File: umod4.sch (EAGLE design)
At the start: 94 parts, among them IC3 27C256-FEED-THRU, J1 DM3AT-SF-PEJ, J2 10118194-0001LF, M1 RPi Pico W, M2 Generic single-sided NEO-8, Q1 C10487/SI2301CDS, Q2 SS8050, Q3 C10487/SI2301CDS, Q4 C10487/SI2301CDS, U1 74LVC541, U2 74LVC4245, U3 74LVC541, U4 RP2040, U5 W25Q128JVSIQ, U6 74LVC2G04, U8 3.3V/150mA, Y1 12MHz

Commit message: 4v2a Release: add caps, DNP convention, production automation
Board changes:
- See Changelist-4V2.md for details

Tooling:
- Add preproduction.py: BOM generation (HTML + CSV), CPL generation via Eagle ULP batch mode, gerber freshness check, and ZIP packaging
- Add jlcpcb_smta_exporter_v7.ulp: modified to accept batch-mode arguments, bypassing interactive dialogs when invoked from script
- Update jlcpcb_2_layer_v72.cam: output path changed to build/cam/
- Update .gitignore: build/ directory rules with build/cam/.gitkeep anchor

Documentation:
- Add Production.md: describes end-to-end JLCPCB submission workflow
- Remove TestPlan.md
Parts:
- removed D4: C2761795/WS2812B, SparkFun-LED:WS2812B
- removed J2: 10118194-0001LF, 10118194-0001LF:10118194-0001LF
- removed JP5, JP6: JUMPER-SMT_3_1-NC_TRACE_NO-SILK, SparkFun-Jumpers:JUMPER-SMT_3_1-NC_TRACE_NO-SILK
- removed Q3, Q4: C10487/SI2301CDS, robins-v7:FET-P-CHANNELSI2369DS
- removed S1: (no value), robins-v7:SWITCH-TAC-5.2MM
- added C25: 100n/16V/X7R, SparkFun-03-01-2010:CAP0402-CAP
- added LED5: WS2812, SparkFun-LED:WS2812B
- added LED7: NCD0805R1, led:LEDSML0805
- added R26: 10K, SparkFun-03-01-2010:RESISTOR0402-RES
- added R27: 1K, SparkFun-03-01-2010:RESISTOR0402-RES
- added R28: 470R, SparkFun-03-01-2010:RESISTOR0402-RES
- added TP10, TP11, TP12, TP13, TP14, TP15, TP16: 1035, robins-v7:TEST-POINT-1035
- added U7: 74LVC4245, robins-v7:74LVC4245-TSSOP24
- C10, C3: value 100n/16V/X7R -> 2u2/6.3V/X5R; LCSC_PART C1525 -> C12530
- C11: value 100n/16V/X7R -> 33p/6.3V/COG; LCSC_PART C1525 -> C1562
- C13: value 1u/25V/X5R -> 4u7/10V/X5R; LCSC_PART C52923 -> C23733
- C16, C24: value 100n/16V/X7R -> 10u/25V/X5R; device SparkFun-03-01-2010:CAP0402-CAP -> robins-v7:CAP-0805; LCSC_PART C1525 -> C15850
- C17: value 33p/6.3V/COG -> 10u/25V/X5R; device SparkFun-03-01-2010:CAP0402-CAP -> robins-v7:CAP-0805; LCSC_PART C1562 -> C15850
- C2, C28: value 1u/25V/X5R -> 100n/16V/X7R; LCSC_PART C52923 -> C1525
- C20, C22: value 2u2/6.3V/X5R -> 100n/16V/X7R; LCSC_PART C12530 -> C1525
- C21: value 2u2/6.3V/X5R -> 1u/25V/X5R; LCSC_PART C12530 -> C52923
- C23: value 100n/16V/X7R -> 1u/25V/X5R; LCSC_PART C1525 -> C52923
- C26: value 100n/16V/X7R -> 4u7/10V/X5R; LCSC_PART C1525 -> C23733
- C27: value 4u7/10V/X5R -> 100n/16V/X7R; LCSC_PART C23733 -> C1525
- C4: value 1u/25V/X5R -> 2u2/6.3V/X5R; LCSC_PART C52923 -> C12530
- D2: value C2761795/WS2812B -> 1N5819WS; device SparkFun-LED:WS2812B -> SparkFun-DiscreteSemi:DIODE-SCHOTTKY-BAT20J; LCSC_PART C2761795 -> C191023
- JP1: value PINHD-1X12 -> (none); device robins:PINHD-1X12 -> pinhead:PINHD-1X3
- JP4: value (none) -> PINHD-1X12; device pinhead:PINHD-1X3 -> robins:PINHD-1X12
- LED3: value KT-0805G -> KT-0805Y; LCSC_PART C2297 -> C2296
- LED6: value C2761795/WS2812B -> WS2812; LCSC_PART C2761795 -> C42417498
- M1: value RPi Pico W -> Generic single-sided NEO-8; device robins-v7:PICO-OR-PICOW'-PICO-OR-W' -> robins-v7:GPS-GENERIC-DS-DBL-SIDED
- M2: value Generic single-sided NEO-8 -> RPi Pico W; device robins-v7:GPS-GENERIC-DS-DBL-SIDED -> robins-v7:PICO-OR-PICOW'-PICO-OR-W'
- Q1: value C10487/SI2301CDS -> DNP/SI2301CDS; DNP_LCSC_PART (none) -> C10487; LCSC_PART C10487 -> (none)
- R1: value 1K -> 100R; device SparkFun-03-01-2010:RESISTOR0402-RES -> SparkFun-03-01-2010:RESISTOR0603-RES; LCSC_PART C11702 -> C22775
- R10: value 27R -> 1K; LCSC_PART C25100 -> C11702
- R11, R18: value 27R -> 10K; LCSC_PART C25100 -> C25744
- R13, R25: value 1K -> 10K; LCSC_PART C11702 -> C25744
- R14, R6: value 10K -> 1K; LCSC_PART C25744 -> C11702
- R2: device SparkFun-03-01-2010:RESISTOR0402-RES -> SparkFun-03-01-2010:RESISTOR0603-RES; LCSC_PART (none) -> C22775
- R20: value 470R -> 100R; device SparkFun-03-01-2010:RESISTOR0402-RES -> SparkFun-03-01-2010:RESISTOR0603-RES; LCSC_PART C25117 -> C22775
- R23: value 1K -> 470R; LCSC_PART C11702 -> C25117
- R24: value 10K -> 470R; LCSC_PART C25744 -> C25117
- R4: value 1K -> 4K7; device SparkFun-03-01-2010:RESISTOR0402-RES -> SparkFun-03-01-2010:RESISTOR0603-RES; LCSC_PART C11702 -> C23162
- R7: value 470R -> 10K; LCSC_PART C25117 -> C25744
- R9: value 100R -> 10K; LCSC_PART (none) -> C25744
- SD1: value DM3AT-SF-PEJ -> DM3AT-SF-PEJM5; LCSC_PART (none) -> C114218; SKIP_LCSC_PART C114218 -> (none)
- TP1, TP2, TP3, TP4, TP5, TP6, TP7, TP8, TP9: value (none) -> 1035
- U1: value 74LVC541 -> RP2040; device robins-v7:74XX541-TSSOP20 -> robins-v7:RP2040-QFN56; LCSC_PART C113281 -> C2040
- U2: value 74LVC4245 -> W25Q128JVSIQ; device robins-v7:74LVC4245-TSSOP24 -> SparkFun-IC-Memory:W25Q32FVSS; LCSC_PART C6091 -> C97521
- U3: value 74LVC541 -> SY6280AAC; device robins-v7:74XX541-TSSOP20 -> robins-v7:HI-SIDE-SW; LCSC_PART C113281 -> C55136
- U4: value RP2040 -> 74LVC2G04; device robins-v7:RP2040-QFN56 -> robins-v7:74LVC2G04-SOT23-6; LCSC_PART C2040 -> C10428
- U5: value W25Q128JVSIQ -> 74LVC541; device SparkFun-IC-Memory:W25Q32FVSS -> robins-v7:74XX541-TSSOP20; LCSC_PART C97521 -> C113281
- U6: value 74LVC2G04 -> 74LVC541; device robins-v7:74LVC2G04-SOT23-6 -> robins-v7:74XX541-TSSOP20; LCSC_PART C10428 -> C113281
- U8: value 3.3V/150mA -> TLV75733P; LCSC_PART (none) -> C485517
- renumbered D3 to LED6, IC3 to IC1, J1 to SD1
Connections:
- removed net 3V3_GPS_EN: M1.GP5, R22.1, R23.2
- removed net 3V3_SD_EN: M1.GP22, R24.2, R25.1
- removed net 3V3_SD_SW: JP5.3, Q4.S
- removed net 3V3_SW: JP6.3, Q3.S
- removed net N$15: R10.2, U4.USB_DP
- removed net N$16: R9.1, U4.SWD
- removed net N$17: J2.2, R11.1
- removed net N$18: J2.3, R10.1
- removed net N$23: Q4.G, R25.2
- removed net N$25: Q3.G, R23.1
- removed net SPARE0: LED3.C, M1.GP27, TP7.TP
- removed net SPARE1: LED4.C, M1.GP26, TP8.TP
- removed net SPARE2: M1.GP16, TP9.TP
- removed net VCC_GPS: JP6.2, M2.VCC, R8.2
- new net DISK_BSY: LED1.C, M2.GP26, TP5.TP
- new net EN_VDD_SD: M2.GP19, R17.1, U3.EN
- new net EP_BOOTSEL: M2.GP21, R6.2
- new net EP_SWD_DIS: JP3.1, M2.GP5
- new net EXT_RP_SWCLK: JP1.1, R1.2
- new net EXT_RP_SWD: JP1.3, R2.2
- new net SPARE0_ADC: M2.GP27, TP9.TP
- new net SPARE3: LED2.C, M2.GP16, TP10.TP
- new net SPARE4: LED7.C, M2.GP17, TP8.TP
- new net SPARE5: M2.GP18, TP6.TP
- new net SPARE6_ADC: M2.GP28, TP15.TP
- new net VCCB_PWR: M2.GP20, R26.2
- new net VLED: C27.1, C28.1, D2.C, LED5.VDD, LED6.VDD
- net !CARD: now also M2.GP6; no longer M1.GP6
- net !CE!_5V: now also R22.1, U4G$2.I, U7.!OE; no longer R6.1, U2.!OE, U6G$2.I
- net !RESET!_5V: now also JP4.6; no longer JP1.6
- net !RESET!_HC11_OUT: now also R25.1, U1.GPIO28_ADC2; no longer M1.GP28, R5.1, U4.GPIO28_ADC2
- net +3V3: now also C14.1, C17.1, C2.1, C4.1, C5.1, C6.1, C8.1, M1.VCC, M2.3V3(OUT), M2.ADC_REF, R11.1, R12.1, R19.2, R23.1, R24.1, R25.2, R28.1, R4.1, R7.2, U1.ADC_AVDD, U1.IOVDD0, U1.IOVDD1, U1.IOVDD2, U1.IOVDD3, U1.IOVDD4, U1.IOVDD5, U1.USB_VDD, U1.VREG_IN, U2.VCC, U3.IN; no longer C11.1, C12.1, C19.1, C20.1, C22.1, JP5.1, JP6.1, M1.3V3(OUT), M1.ADC_REF, Q3.D, Q4.D, R12.2, R17.1, R19.1, R20.1, R22.2, R3.2, R7.1, U4.ADC_AVDD, U4.IOVDD0, U4.IOVDD1, U4.IOVDD2, U4.IOVDD3, U4.IOVDD4, U4.IOVDD5, U4.USB_VDD, U4.VREG_IN, U5.VCC
- net +5_ECU: now also C25.1, C26.1, JP4.10, JP4.12, R22.2, U7.VCCA; no longer C28.1, C5.1, JP1.10, JP1.12, R6.2, U2.VCCA
- net 1.0V: now also C1.1, C3.1, U1.DVDD0, U1.DVDD1, U1.VREG_OUT; no longer C21.1, C8.1, U4.DVDD0, U4.DVDD1, U4.VREG_OUT
- net A0_5V: now also U5.A1; no longer U1.A1
- net A10_5V: now also U6.A3; no longer U3.A3
- net A11_5V: now also U6.A4; no longer U3.A4
- net A12_5V: now also U6.A5; no longer U3.A5
- net A13_5V: now also U6.A6; no longer U3.A6
- net A14_5V: now also U6.A7; no longer U3.A7
- net A1_5V: now also U5.A2; no longer U1.A2
- net A2_5V: now also U5.A3; no longer U1.A3
- net A3_5V: now also U5.A4; no longer U1.A4
- net A4_5V: now also U5.A5; no longer U1.A5
- net A5_5V: now also U5.A6; no longer U1.A6
- net A6_5V: now also U5.A7; no longer U1.A7
- net A7_5V: now also U5.A8; no longer U1.A8
- net A8_5V: now also U6.A1; no longer U3.A1
- net A9_5V: now also U6.A2; no longer U3.A2
- net CE: now also U1.GPIO26_ADC0, U4G$2.O; no longer U4.GPIO26_ADC0, U6G$2.O
- net D0: now also U1.GPIO16, U7.B1; no longer U2.B1, U4.GPIO16
- net D0_5V: now also U7.A1; no longer U2.A1
- net D1: now also U1.GPIO17, U7.B2; no longer U2.B2, U4.GPIO17
- net D1_5V: now also U7.A2; no longer U2.A2
- net D2: now also U1.GPIO18, U7.B3; no longer U2.B3, U4.GPIO18
- net D2_5V: now also U7.A3; no longer U2.A3
- net D3: now also U1.GPIO19, U7.B4; no longer U2.B4, U4.GPIO19
- net D3_5V: now also U7.A4; no longer U2.A4
- net D4: now also U1.GPIO20, U7.B5; no longer U2.B5, U4.GPIO20
- net D4_5V: now also U7.A5; no longer U2.A5
- net D5: now also U1.GPIO21, U7.B6; no longer U2.B6, U4.GPIO21
- net D5_5V: now also U7.A6; no longer U2.A6
- net D6: now also U1.GPIO22, U7.B7; no longer U2.B7, U4.GPIO22
- net D6_5V: now also U7.A7; no longer U2.A7
- net D7: now also U1.GPIO23, U7.B8; no longer U2.B8, U4.GPIO23
- net D7_5V: now also U7.A8; no longer U2.A8
- net DAT1: now also M2.GP13, R8.1; no longer M1.GP13, R16.1
- net DAT2: now also M2.GP14; no longer M1.GP14
- net DBG_BSY: now also LED4.C, TP14.TP, U1.GPIO29_ADC3; no longer D4.DI, LED1.C, TP1.TP, U4.GPIO29_ADC3
- net E: now also R20.1, U1.GPIO15; no longer R18.1, U4.GPIO15
- net EP_RUN: now also M2.GP4, R19.1, U1.RUN; no longer M1.GP4, R3.1, U4.RUN
- net E_5V: now also JP4.9, TP11.TP, U6.A8; no longer JP1.9, TP5.TP, U3.A8
- net GND: now also C11.1, C17.2, C25.2, JP1.2, JP3.2, JP4.1, JP4.3, LED3.C, LED5.VSS, M2.SWGND, R16.2, R17.2, R18.2, R3.2, TP1.TP, TP13.TP, TP16.TP, TP7.TP, U1.TESTEN, U2.GND, U4G$3.GND, U5.!OE1, U5.!OE2, U6.!OE1, U6.!OE2, U6.GND, U7.GND@1, U7.GND@2, U7.GND@3; no longer C11.2, C17.1, D2.VSS, D4.VSS, J2.5, JP1.1, JP1.3, JP4.2, LED2.C, M1.SWGND, R13.2, R14.2, R24.1, TP2.TP, TP3.TP, TP4.TP, U1.!OE1, U1.!OE2, U2.GND@1, U2.GND@2, U2.GND@3, U3.!OE1, U3.!OE2, U4.GND, U4.TESTEN, U6G$3.GND
- net GPS_PPS: now also M1.PPS, M2.GP7; no longer M1.GP7, M2.PPS
- net IO0: now also U1.GPIO0, U5.Y1; no longer U1.Y1, U4.GPIO0
- net IO1: now also U1.GPIO1, U5.Y2; no longer U1.Y2, U4.GPIO1
- net IO10: now also U1.GPIO10, U6.Y3; no longer U3.Y3, U4.GPIO10
- net IO11: now also U1.GPIO11, U6.Y4; no longer U3.Y4, U4.GPIO11
- net IO12: now also U1.GPIO12, U6.Y5; no longer U3.Y5, U4.GPIO12
- net IO13: now also U1.GPIO13, U6.Y6; no longer U3.Y6, U4.GPIO13
- net IO14: now also U1.GPIO14, U6.Y7; no longer U3.Y7, U4.GPIO14
- net IO2: now also U1.GPIO2, U5.Y3; no longer U1.Y3, U4.GPIO2
- net IO3: now also U1.GPIO3, U5.Y4; no longer U1.Y4, U4.GPIO3
- net IO4: now also U1.GPIO4, U5.Y5; no longer U1.Y5, U4.GPIO4
- net IO5: now also U1.GPIO5, U5.Y6; no longer U1.Y6, U4.GPIO5
- net IO6: now also U1.GPIO6, U5.Y7; no longer U1.Y7, U4.GPIO6
- net IO7: now also U1.GPIO7, U5.Y8; no longer U1.Y8, U4.GPIO7
- net IO8: now also U1.GPIO8, U6.Y1; no longer U3.Y1, U4.GPIO8
- net IO9: now also U1.GPIO9, U6.Y2; no longer U3.Y2, U4.GPIO9
- net N$1: now also R10.2; no longer R4.2
- net N$10: now also U1.QSPI_SD1, U2.SO(D1); no longer U4.QSPI_SD1, U5.SO(D1)
- net N$11: now also U1.QSPI_SD2, U2.!WP!(D2); no longer U4.QSPI_SD2, U5.!WP!(D2)
- net N$12: now also U1.QSPI_SD3, U2.!HOLD!(D3); no longer U4.QSPI_SD3, U5.!HOLD!(D3)
- net N$13: now also LED2.A, R23.2; no longer R11.2, U4.USB_DM
- net N$14: now also R16.1, U3.ISET; no longer R13.1, S1.1
- net N$19: now also LED5.DI; no longer D2.DI
- net N$2: now also C11.2, U1.XIN; no longer C17.2, U4.XIN
- net N$20: now also R20.2, U6.Y8; no longer R18.2, U3.Y8
- net N$21: now also LED1.A, R21.2; no longer LED3.A, R20.2
- net N$22: now also LED7.A, R28.2; no longer LED4.A, R21.2
- net N$3: now also LED3.A, R27.2; no longer LED2.A, R1.2
- net N$4: now also R14.1, TP4.TP; no longer R2.1, U4.SWCLK
- net N$5: now also R10.1, U1.XOUT; no longer R4.1, U4.XOUT
- net N$6: now also LED4.A, R24.2; no longer LED1.A, R7.2
- net N$7: now also R14.2, R6.1, R7.1, U1.QSPI_SS, U2.!CS!; no longer R12.1, S1.2, U4.QSPI_SS, U5.!CS!
- net N$8: now also U1.QSPI_SCLK, U2.SCK; no longer U4.QSPI_SCLK, U5.SCK
- net N$9: now also U1.QSPI_SD0, U2.SI(D0); no longer U4.QSPI_SD0, U5.SI(D0)
- net PICOW_U0_RX: now also M2.GP1, R11.2, TP2.TP, U1.GPIO24; no longer JP3.1, M1.GP1, R17.2, U4.GPIO24
- net PICOW_U0_TX: now also M2.GP0, R12.2, TP3.TP, U1.GPIO25; no longer JP3.2, M1.GP0, R19.2, U4.GPIO25
- net PICOW_U1_RX: now also M1.TX_OUT, M2.GP9; no longer M1.GP9, M2.TX_OUT
- net PICOW_U1_TX: now also M1.RX_IN, M2.GP8, R5.1; no longer M1.GP8, M2.RX_IN, R8.1
- net R/!W!_5V: now also JP4.8, TP12.TP, U4G$1.I; no longer JP1.8, TP6.TP, U6G$1.I
- net RP_SWCLK: now also M2.GP2, R1.1, R3.1, U1.SWCLK; no longer JP4.1, M1.GP2, R2.2
- net RP_SWD: now also M2.GP3, R2.1, R4.2, U1.SWD; no longer JP4.3, M1.GP3, R9.2
- net SPI1_CS: now also M2.GP15, R13.1; no longer M1.GP15
- net SPI1_MISO: now also M2.GP12, R9.1; no longer M1.GP12
- net SPI1_MOSI: now also M2.GP11; no longer M1.GP11
- net SPI1_SCK: now also M2.GP10, R18.1; no longer M1.GP10, R14.1
- net VBUS: now also M2.VBUS; no longer M1.VBUS
- net VCCB: now also C19.1, C20.1, C21.1, C22.1, C23.1, C24.1, R26.1, R27.1, U4G$3.VCC, U5.VCC, U6.VCC, U7.VCCB@1, U7.VCCB@2; no longer C1.1, C13.1, C2.1, C3.1, C4.1, C6.1, R1.1, U1.VCC, U2.VCCB@1, U2.VCCB@2, U3.VCC, U6G$3.VCC
- net VDD_SD: now also C12.1, C13.1, R13.2, R8.2, R9.2, U3.OUT; no longer C14.1, C27.1, JP5.2, R16.2
- net VSYS: now also D2.A, M2.VSYS; no longer C23.1, C24.1, C26.1, D2.VDD, D4.VDD, LED6.VDD, M1.VSYS
- net W/!R!: now also U1.GPIO27_ADC1, U4G$1.O, U7.DIR; no longer U2.DIR, U4.GPIO27_ADC1, U6G$1.O
- net WP_RUN: now also M2.RUN; no longer M1.RUN
- net WS2812_DI: now also M2.GP22; no longer M1.GP21
- net XIRQ_5V: now also JP4.4; no longer JP1.4
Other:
- note added: "ADC Capable"
- note added: "FET Q1 is optional Leaving it unstuffed increases the load on the ECU power supply a tiny bit, but leaving the FET out is one less part to break."
- note added: "GRN"
- note added: "RED"
- note added: "YEL"
- note removed: "BOOTSEL"
- note removed: "Default is that the RP2040 runs at boot, but can be reset by the Pico W if desired."
- note removed: "Default is to power SD Card via 3V3_SD_SW. If desired, cut the jumper and solder the other side to power SD card permanently via +3V3."
- note removed: "Default: DISABLED '1': ENABLED"
- note removed: "Default: ENABLED '0': DISABLED"

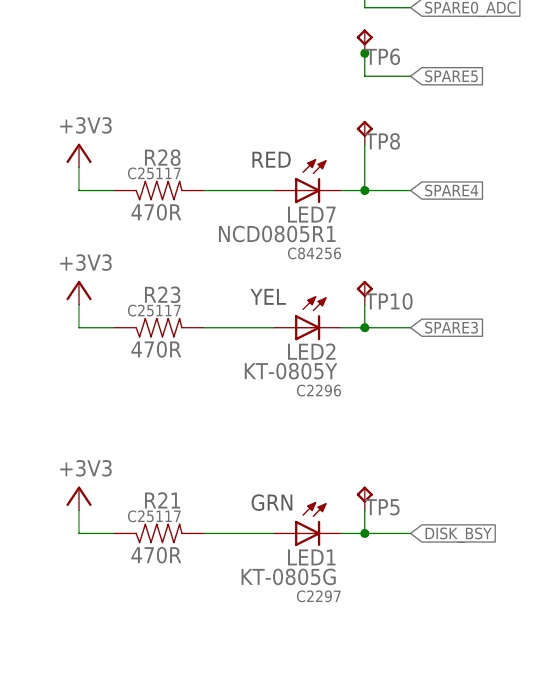
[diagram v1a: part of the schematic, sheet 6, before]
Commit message: Replace 470R 0402 package with SMD-0603-NOM
- Affected parts: R21, R23, R24, R28
- LCSC_PART changes from C25117 to C23179
- Manually reworked wire angles on board to clear DRC failures
  from the new pad geometry
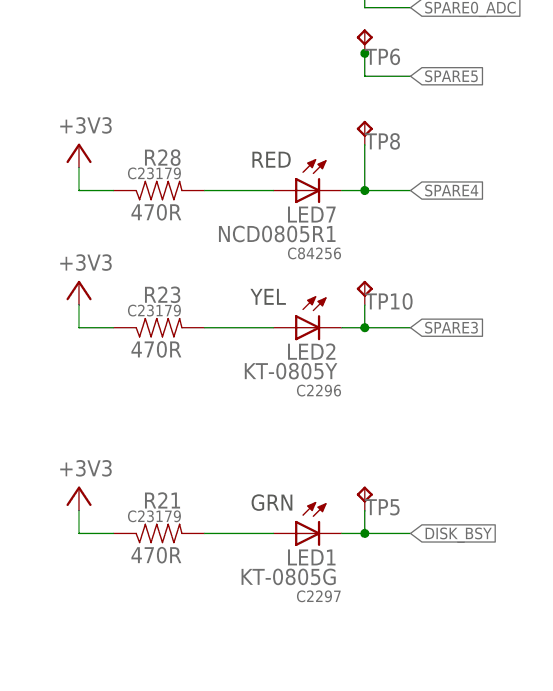
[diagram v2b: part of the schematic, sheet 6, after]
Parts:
- R21, R23, R24, R28: device SparkFun-03-01-2010:RESISTOR0402-RES -> robins-v7:RES-0603-NOM; LCSC_PART C25117 -> C23179
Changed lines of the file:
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@@
 <grid distance="0.1" unitdist="inch" unit="inch" style="lines" multiple="1" display="no" altdistance="0.01" altunitdist="inch" altunit="inch"/>
 <layers>
-<layer number="1" name="Top" color="4" fill="1" visible="yes" active="no"/>
-<layer number="2" name="Route2" color="1" fill="3" visible="yes" active="no"/>
-<layer number="3" name="Route3" color="4" fill="3" visible="yes" active="no"/>
-<layer number="14" name="Route14" color="1" fill="6" visible="yes" active="no"/>
-<layer number="15" name="Route15" color="4" fill="6" visible="yes" active="no"/>
-<layer number="16" name="Bottom" color="1" fill="1" visible="yes" active="no"/>
-<layer number="17" name="Pads" color="2" fill="1" visible="yes" active="no"/>
-<layer number="18" name="Vias" color="2" fill="1" visible="yes" active="no"/>
-<layer number="19" name="Unrouted" color="6" fill="1" visible="yes" active="no"/>
-<layer number="20" name="Dimension" color="15" fill="1" visible="yes" active="no"/>
-<layer number="21" name="tPlace" color="7" fill="1" visible="yes" active="no"/>
-<layer number="22" name="bPlace" color="7" fill="1" visible="yes" active="no"/>
-<layer number="23" name="tOrigins" color="15" fill="1" visible="yes" active="no"/>
-<layer number="24" name="bOrigins" color="15" fill="1" visible="yes" active="no"/>
-<layer number="25" name="tNames" color="7" fill="1" visible="yes" active="no"/>
-<layer number="26" name="bNames" color="7" fill="1" visible="yes" active="no"/>
-<layer number="27" name="tValues" color="7" fill="1" visible="yes" active="no"/>
-<layer number="28" name="bValues" color="7" fill="1" visible="yes" active="no"/>
+<layer number="1" name="Top" color="4" fill="1" visible="no" active="no"/>
+<layer number="2" name="Route2" color="1" fill="3" visible="no" active="no"/>
+<layer number="3" name="Route3" color="4" fill="3" visible="no" active="no"/>
+<layer number="14" name="Route14" color="1" fill="6" visible="no" active="no"/>
+<layer number="15" name="Route15" color="4" fill="6" visible="no" active="no"/>
+<layer number="16" name="Bottom" color="1" fill="1" visible="no" active="no"/>
+<layer number="17" name="Pads" color="2" fill="1" visible="no" active="no"/>
+<layer number="18" name="Vias" color="2" fill="1" visible="no" active="no"/>
+<layer number="19" name="Unrouted" color="6" fill="1" visible="no" active="no"/>
+<layer number="20" name="Dimension" color="15" fill="1" visible="no" active="no"/>
+<layer number="21" name="tPlace" color="7" fill="1" visible="no" active="no"/>
+<layer number="22" name="bPlace" color="7" fill="1" visible="no" active="no"/>
+<layer number="23" name="tOrigins" color="15" fill="1" visible="no" active="no"/>
+<layer number="24" name="bOrigins" color="15" fill="1" visible="no" active="no"/>
+<layer number="25" name="tNames" color="7" fill="1" visible="no" active="no"/>
+<layer number="26" name="bNames" color="7" fill="1" visible="no" active="no"/>
+<layer number="27" name="tValues" color="7" fill="1" visible="no" active="no"/>
+<layer number="28" name="bValues" color="7" fill="1" visible="no" active="no"/>
 <layer number="29" name="tStop" color="7" fill="3" visible="no" active="no"/>
 <layer number="30" name="bStop" color="7" fill="6" visible="no" active="no"/>
@@
 <layer number="35" name="tGlue" color="7" fill="4" visible="no" active="no"/>
 <layer number="36" name="bGlue" color="7" fill="5" visible="no" active="no"/>
-<layer number="37" name="tTest" color="7" fill="1" visible="yes" active="no"/>
-<layer number="38" name="bTest" color="7" fill="1" visible="yes" active="no"/>
+<layer number="37" name="tTest" color="7" fill="1" visible="no" active="no"/>
+<layer number="38" name="bTest" color="7" fill="1" visible="no" active="no"/>
 <layer number="39" name="tKeepout" color="4" fill="11" visible="no" active="no"/>
 <layer number="40" name="bKeepout" color="1" fill="11" visible="no" active="no"/>
@@
 <layer number="44" name="Drills" color="7" fill="1" visible="no" active="no"/>
 <layer number="45" name="Holes" color="7" fill="1" visible="no" active="no"/>
-<layer number="46" name="Milling" color="3" fill="1" visible="yes" active="no"/>
-<layer number="47" name="Measures" color="7" fill="1" visible="yes" active="no"/>
-<layer number="48" name="Document" color="7" fill="1" visible="yes" active="no"/>
-<layer number="49" name="Reference" color="7" fill="1" visible="yes" active="no"/>
-<layer number="50" name="dxf" color="7" fill="1" visible="yes" active="no"/>
-<layer number="51" name="tDocu" color="7" fill="1" visible="yes" active="no"/>
-<layer number="52" name="bDocu" color="7" fill="1" visible="yes" active="no"/>
-<layer number="53" name="tGND_GNDA" color="7" fill="9" visible="yes" active="no"/>
-<layer number="54" name="bGND_GNDA" color="1" fill="9" visible="yes" active="no"/>
-<layer number="56" name="wert" color="7" fill="1" visible="yes" active="no"/>
-<layer number="57" name="tCAD" color="7" fill="1" visible="yes" active="no"/>
-<layer number="59" name="tCarbon" color="7" fill="1" visible="yes" active="no"/>
-<layer number="60" name="bCarbon" color="7" fill="1" visible="yes" active="no"/>
+<layer number="46" name="Milling" color="3" fill="1" visible="no" active="no"/>
+<layer number="47" name="Measures" color="7" fill="1" visible="no" active="no"/>
+<layer number="48" name="Document" color="7" fill="1" visible="no" active="no"/>
+<layer number="49" name="Reference" color="7" fill="1" visible="no" active="no"/>
+<layer number="50" name="dxf" color="7" fill="1" visible="no" active="no"/>
+<layer number="51" name="tDocu" color="7" fill="1" visible="no" active="no"/>
+<layer number="52" name="bDocu" color="7" fill="1" visible="no" active="no"/>
+<layer number="53" name="tGND_GNDA" color="7" fill="9" visible="no" active="no"/>
+<layer number="54" name="bGND_GNDA" color="1" fill="9" visible="no" active="no"/>
+<layer number="56" name="wert" color="7" fill="1" visible="no" active="no"/>
+<layer number="57" name="tCAD" color="7" fill="1" visible="no" active="no"/>
+<layer number="59" name="tCarbon" color="7" fill="1" visible="no" active="no"/>
+<layer number="60" name="bCarbon" color="7" fill="1" visible="no" active="no"/>
 <layer number="88" name="SimResults" color="9" fill="1" visible="yes" active="yes"/>
 <layer number="89" name="SimProbes" color="9" fill="1" visible="yes" active="yes"/>
@@
 <attribute name="LCSC_PART" value="C25744"/>
 </part>
-<part name="R24" library="SparkFun-03-01-2010" deviceset="RESISTOR" device="0402-RES" value="470R">
-<attribute name="LCSC_PART" value="C25117"/>
+<part name="R24" library="robins-v7" deviceset="RES" device="-0603-NOM" value="470R">
+<attribute name="LCSC_PART" value="C23179"/>
 </part>
 <part name="+3V14" library="supply1" deviceset="+3V3" device=""/>
@@
 <part name="V26" library="supply2" deviceset="GND" device=""/>
 <part name="V31" library="supply2" deviceset="GND" device=""/>
-<part name="R21" library="SparkFun-03-01-2010" deviceset="RESISTOR" device="0402-RES" value="470R">
-<attribute name="LCSC_PART" value="C25117"/>
+<part name="R21" library="robins-v7" deviceset="RES" device="-0603-NOM" value="470R">
+<attribute name="LCSC_PART" value="C23179"/>
 </part>
 <part name="+3V2" library="supply1" deviceset="+3V3" device=""/>
@@
 <attribute name="LCSC_PART" value="C2297"/>
 </part>
-<part name="R28" library="SparkFun-03-01-2010" deviceset="RESISTOR" device="0402-RES" value="470R">
-<attribute name="LCSC_PART" value="C25117"/>
+<part name="R28" library="robins-v7" deviceset="RES" device="-0603-NOM" value="470R">
+<attribute name="LCSC_PART" value="C23179"/>
 </part>
 <part name="+3V3" library="supply1" deviceset="+3V3" device=""/>
@@
 </part>
 <part name="TP6" library="robins-v7" deviceset="TEST-POINT" device="-1035" value="1035"/>
-<part name="R23" library="SparkFun-03-01-2010" deviceset="RESISTOR" device="0402-RES" value="470R">
-<attribute name="LCSC_PART" value="C25117"/>
+<part name="R23" library="robins-v7" deviceset="RES" device="-0603-NOM" value="470R">
+<attribute name="LCSC_PART" value="C23179"/>
 </part>
 <part name="+3V17" library="supply1" deviceset="+3V3" device=""/>

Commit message: Replace 1K 0402 packages with SMD-0603-NOM
- Affected parts: R6, R10, R14, R27
- LCSC_PART changes from C11702 to C21190
- Manually reworked wire angles on board to clear DRC failures from the new pad geometry
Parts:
- R10, R14, R27, R6: device SparkFun-03-01-2010:RESISTOR0402-RES -> robins-v7:RES-0603-NOM; LCSC_PART C11702 -> C21190
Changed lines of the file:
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@@
 <attribute name="LCSC_PART" value="C9002"/>
 </part>
-<part name="R10" library="SparkFun-03-01-2010" deviceset="RESISTOR" device="0402-RES" value="1K">
-<attribute name="LCSC_PART" value="C11702"/>
+<part name="R10" library="robins-v7" deviceset="RES" device="-0603-NOM" value="1K">
+<attribute name="LCSC_PART" value="C21190"/>
 </part>
 <part name="C11" library="SparkFun-03-01-2010" deviceset="CAP" device="0402-CAP" value="33p/6.3V/COG">
@@
 </part>
 <part name="V37" library="supply2" deviceset="GND" device=""/>
-<part name="R27" library="SparkFun-03-01-2010" deviceset="RESISTOR" device="0402-RES" value="1K">
-<attribute name="LCSC_PART" value="C11702"/>
+<part name="R27" library="robins-v7" deviceset="RES" device="-0603-NOM" value="1K">
+<attribute name="LCSC_PART" value="C21190"/>
 </part>
 <part name="R1" library="SparkFun-03-01-2010" deviceset="RESISTOR" device="0603-RES" value="100R">
@@
 <attribute name="LCSC_PART" value="C2296"/>
 </part>
-<part name="R6" library="SparkFun-03-01-2010" deviceset="RESISTOR" device="0402-RES" value="1K">
-<attribute name="LCSC_PART" value="C11702"/>
+<part name="R6" library="robins-v7" deviceset="RES" device="-0603-NOM" value="1K">
+<attribute name="LCSC_PART" value="C21190"/>
 </part>
 <part name="R3" library="SparkFun-03-01-2010" deviceset="RESISTOR" device="0402-RES" value="10K">
@@
 <attribute name="LCSC_PART" value="C23733"/>
 </part>
-<part name="R14" library="SparkFun-03-01-2010" deviceset="RESISTOR" device="0402-RES" value="1K">
-<attribute name="LCSC_PART" value="C11702"/>
+<part name="R14" library="robins-v7" deviceset="RES" device="-0603-NOM" value="1K">
+<attribute name="LCSC_PART" value="C21190"/>
 </part>
 <part name="TP15" library="robins-v7" deviceset="TEST-POINT" device="-1035" value="1035"/>

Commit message: Replace 4K7 0603 packages with SMD-0603-NOM
- Affected parts: R4
- LCSC_PART is unchanged
- Manually reworked wire angles on board to clear DRC failures from the new pad geometry
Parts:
- R4: device SparkFun-03-01-2010:RESISTOR0603-RES -> robins-v7:RES-0603-NOM
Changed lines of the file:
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@@
 </part>
 <part name="V2" library="supply2" deviceset="GND" device=""/>
-<part name="R4" library="SparkFun-03-01-2010" deviceset="RESISTOR" device="0603-RES" value="4K7">
+<part name="R4" library="robins-v7" deviceset="RES" device="-0603-NOM" value="4K7">
 <attribute name="LCSC_PART" value="C23162"/>
 </part>

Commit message: Replace 100R 0603 packages with SMD-0603-NOM
- Affected parts: R1, R2, R20
- LCSC_PART unchanged
- Manually reworked wire angles on board to clear DRC failures from the new pad geometry
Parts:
- R1, R2, R20: device SparkFun-03-01-2010:RESISTOR0603-RES -> robins-v7:RES-0603-NOM
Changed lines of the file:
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@@
 <part name="+3V23" library="supply1" deviceset="+3V3" device=""/>
 <part name="V38" library="supply2" deviceset="GND" device=""/>
-<part name="R20" library="SparkFun-03-01-2010" deviceset="RESISTOR" device="0603-RES" value="100R">
+<part name="R20" library="robins-v7" deviceset="RES" device="-0603-NOM" value="100R">
 <attribute name="LCSC_PART" value="C22775"/>
 </part>
@@
 <attribute name="LCSC_PART" value="C21190"/>
 </part>
-<part name="R1" library="SparkFun-03-01-2010" deviceset="RESISTOR" device="0603-RES" value="100R">
+<part name="R1" library="robins-v7" deviceset="RES" device="-0603-NOM" value="100R">
 <attribute name="LCSC_PART" value="C22775"/>
 </part>
-<part name="R2" library="SparkFun-03-01-2010" deviceset="RESISTOR" device="0603-RES" value="100R">
+<part name="R2" library="robins-v7" deviceset="RES" device="-0603-NOM" value="100R">
 <attribute name="LCSC_PART" value="C22775"/>
 </part>
